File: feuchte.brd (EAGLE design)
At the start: 100 x 80 mm, 23 parts, among them CON1 CON_PCB_7.5MM_3-POLE, CON2 CON_PCB_7.5MM_3-POLE, IC1 IC_ULN2003AD, IC2 ESD_USB_IP4234CZ6, K1 RELAY_G5LA, K2 RELAY_G5LA, Q1 12MHz, U1 MCU_ATMEGA32U2-AU

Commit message: weiter gelayouted
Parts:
- added R4: 1k, Bauelemente:0603
- moved C9 79.0 mm to (74.5, 75.8)
- moved C8 64.0 mm to (72.4, 67.8)
- moved R1 64.0 mm to (70.0, 72.3)
- moved C10 64.0 mm to (75.3, 62.7)
- moved C5 44.0 mm to (38.9, 54.9), turned to 270 degrees
- moved C7 42.1 mm to (65.0, 72.2)
- moved C4 34.2 mm to (43.1, 65.3)
- moved C6 32.0 mm to (43.1, 66.8)
- moved C3 17.7 mm to (54.9, 64.6), turned to 90 degrees
- moved U$1 15.7 mm to (45.7, 45.3), turned to 0 degrees
- moved C2 15.2 mm to (54.9, 68.3)
- moved Q1 12.8 mm to (49.7, 65.7), flipped to the top
- moved U1 8.86 mm to (46.8, 55.8), turned to 270 degrees
- moved R2 2.19 mm to (39.1, 62.3)
- moved R3 2.19 mm to (40.6, 62.3)
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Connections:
- net USBC_N renamed USBC_
- net USBR_N renamed USBR_
- new net N$20: R4.2, U1.13
- net GND: now also IC1.1, IC1.3, IC1.4, IC1.5, IC1.6, R4.1; no longer U1.13
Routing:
- net +5V: track 56.9 -> 69.4 mm, vias 0 -> 1
- net N$1: track 9.75 -> 0.00 mm
- net USBR_P: track 0.00 -> 7.32 mm
- net USBC_P: track 0.35 -> 7.35 mm
- net N$11: track 2.20 -> 9.09 mm
- net N$12: track 9.50 -> 16.0 mm
- net USBR_: track 0.00 -> 6.30 mm
- net N$2: track 6.08 -> 0.00 mm
- net USBC_: track 0.35 -> 6.22 mm
- net +3V3: track 0.00 -> 3.92 mm
- net GND: track 17.0 -> 19.0 mm
- added copper zone on layer 16, net +5V
- added copper zone on layer 16, net GND

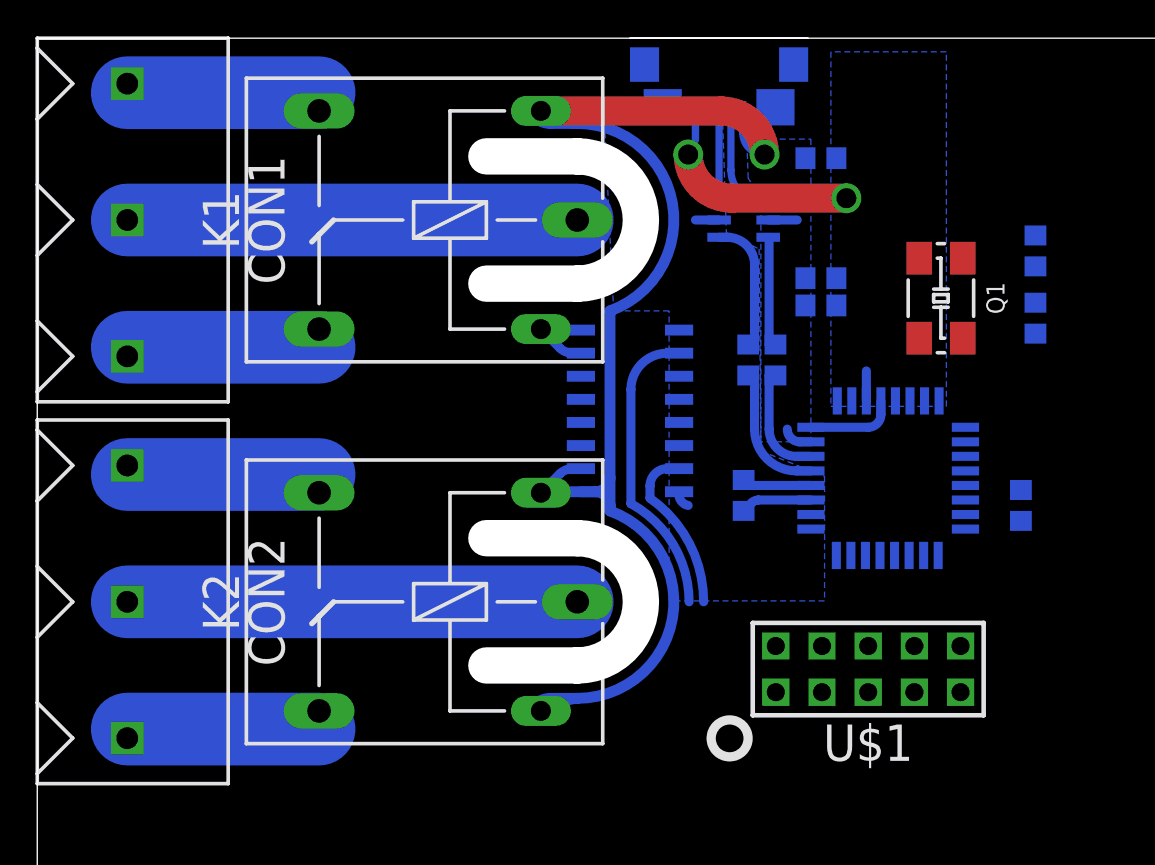
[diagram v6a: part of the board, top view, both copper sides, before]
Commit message: weiter gelayouted, jetzt mit quarz
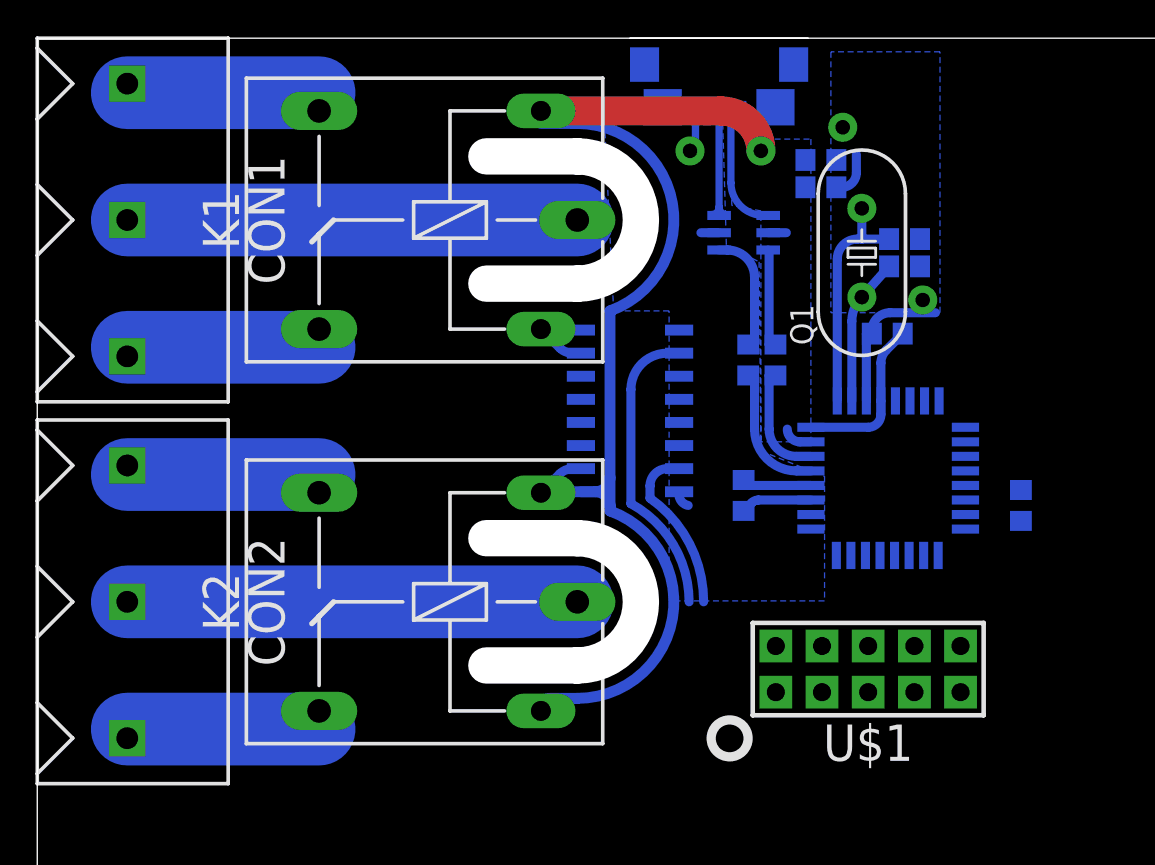
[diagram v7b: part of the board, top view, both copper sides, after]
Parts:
- C1: value 100n -> 10µ
- C6: value 10µ -> 100n
- Q1: value 12MHz -> 16MHz; device Bauelemente:QUARTZ_ABMM2 -> Bauelemente:QUARTZ_HC49S
- moved C3 7.74 mm to (47.7, 67.5), turned to 180 degrees
- moved C2 7.23 mm to (47.7, 69.0), turned to 180 degrees
- moved Q1 5.02 mm to (45.4, 68.2), turned to 90 degrees
- moved C6 5.00 mm to (43.1, 71.8)
- moved C4 3.97 mm to (46.8, 63.8), turned to 0 degrees
- moved IC2 0.70 mm to (38.9, 69.3)
- moved C1 0.10 mm to (43.1, 73.3)
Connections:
- net GND: no longer Q1.2, Q1.4
- net N$1: now also Q1.2; no longer Q1.1
- net N$2: now also Q1.1; no longer Q1.3
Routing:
- net N$1: track 0.00 -> 12.8 mm
- net N$2: track 0.00 -> 8.08 mm
- net +5V: track 69.4 -> 71.0 mm
- net GND: track 19.0 -> 17.9 mm, vias 2 -> 3
- net USBR_P: track 7.32 -> 6.62 mm
- net USBR_: track 6.30 -> 5.60 mm
- net USBCON_N: track 5.92 -> 6.62 mm
- net USBCON_: track 6.06 -> 6.76 mm

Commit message: weiter gelayouted
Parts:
- moved U$1 0.67 mm to (45.4, 44.7)
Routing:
- net +5V: track 71.0 -> 78.3 mm, vias 1 -> 2
- net N$11: track 9.09 -> 4.92 mm
- net N$12: track 16.0 -> 12.5 mm
- net GND: track 17.9 -> 17.0 mm, vias 3 -> 4
- added copper zone on layer 1, net GND
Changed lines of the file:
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@@
 <wire x1="5" y1="56" x2="15.5" y2="56" width="14" layer="42"/>
 <wire x1="5" y1="42" x2="15.5" y2="42" width="14" layer="42"/>
+<wire x1="29.7" y1="49" x2="24.7" y2="49" width="10" layer="41"/>
+<wire x1="29.7" y1="70" x2="24.7" y2="70" width="10" layer="41"/>
+<wire x1="15.5" y1="77" x2="5" y2="77" width="14" layer="41"/>
+<wire x1="5" y1="70" x2="22.4" y2="70" width="14" layer="41"/>
+<rectangle x1="22" y1="63" x2="26.7" y2="65" layer="41"/>
+<rectangle x1="22" y1="75" x2="26.7" y2="77" layer="41"/>
+<wire x1="5" y1="49" x2="22.4" y2="49" width="14" layer="41"/>
+<rectangle x1="22" y1="42" x2="26.7" y2="44" layer="41"/>
+<rectangle x1="22" y1="54" x2="26.7" y2="56" layer="41"/>
+<wire x1="5" y1="63" x2="15.5" y2="63" width="14" layer="41"/>
+<wire x1="5" y1="56" x2="15.5" y2="56" width="14" layer="41"/>
+<wire x1="5" y1="42" x2="15.5" y2="42" width="14" layer="41"/>
 </plain>
 <attributes>
@@
 <element name="USB1" library="Bauelemente" package="CON_MICROUSB_ZX62R-B-5P" value="CON_MICROUSB_ZX62R-B-5P" x="37.5" y="75.2" rot="MR180"/>
 <element name="IC2" library="Bauelemente" package="USB_ESD_IP4234CZ6" value="ESD_USB_IP4234CZ6" x="38.85" y="69.3" rot="MR90"/>
-<element name="U$1" library="Bauelemente" package="CON_ISP_AVR10" value="CON_SPI_AVR10" x="45.7" y="45.3"/>
+<element name="U$1" library="Bauelemente" package="CON_ISP_AVR10" value="CON_SPI_AVR10" x="45.4" y="44.7"/>
 <element name="C7" library="Bauelemente" package="0603" value="100n" x="65" y="72.2" rot="MR0"/>
 <element name="C8" library="Bauelemente" package="0603" value="100n" x="72.4" y="67.8" rot="MR0"/>
@@
 <contactref element="C6" pad="2"/>
 <contactref element="C4" pad="2"/>
-<via x="35.9" y="73.8" extent="1-16" drill="0.8" alwaysstop="yes"/>
+<via x="35.9" y="73.8" extent="1-16" drill="0.8"/>
 <contactref element="U$1" pad="8"/>
 <contactref element="U$1" pad="10"/>
@@
 <vertex x="31.7" y="65"/>
 </polygon>
-<wire x1="35.3" y1="55.055" x2="35.8" y2="54.3" width="0.5" layer="16" curve="90"/>
 <wire x1="42.55" y1="55.4" x2="38.85" y2="55.4" width="0.5" layer="16"/>
 <wire x1="38.85" y1="55.4" x2="38.85" y2="55.7" width="0.5" layer="16"/>
@@
 <polygon width="0.5" layer="16" isolate="0.3">
 <vertex x="43.65" y="79.25"/>
-<vertex x="43.65" y="64.9"/>
+<vertex x="43.65" y="71.3"/>
+<vertex x="45.4" y="71.3"/>
+<vertex x="45.4" y="64.9"/>
 <vertex x="49.65" y="64.9"/>
 <vertex x="49.65" y="79.25"/>
 </polygon>
-<wire x1="48.55" y1="68.95" x2="44.3" y2="75.1" width="0" layer="19" extent="16-16"/>
-<wire x1="48.7" y1="65.6" x2="49.4" y2="64.9" width="0" layer="19" extent="16-16"/>
-<wire x1="42.55" y1="55.4" x2="45.6" y2="60.05" width="0" layer="19" extent="16-16"/>
-<wire x1="43.16" y1="46.57" x2="42.55" y2="55.4" width="0" layer="19" extent="16-16"/>
-<wire x1="45.7" y1="46.57" x2="43.16" y2="46.57" width="0" layer="19" extent="1-1"/>
-<wire x1="48.24" y1="46.57" x2="45.7" y2="46.57" width="0" layer="19" extent="1-1"/>
-<wire x1="50.78" y1="46.57" x2="48.24" y2="46.57" width="0" layer="19" extent="1-1"/>
-<wire x1="54.1" y1="53.45" x2="50.78" y2="46.57" width="0" layer="19" extent="16-16"/>
+<polygon width="0.5" layer="1" isolate="0.5">
+<vertex x="20" y="80"/>
+<vertex x="59.2" y="80" curve="-90"/>
+<vertex x="60" y="79.2"/>
+<vertex x="60" y="39"/>
+<vertex x="20.8" y="39" curve="-90"/>
+<vertex x="20" y="39.8"/>
+</polygon>
+<via x="37.5" y="57.4" extent="1-16" drill="0.8" alwaysstop="yes"/>
+<wire x1="50.48" y1="45.97" x2="54.1" y2="53.45" width="0" layer="19" extent="16-16"/>
 </signal>
 <signal name="N$1">
@@
 <wire x1="40.2" y1="69.3" x2="41.2" y2="69.3" width="0.5" layer="16"/>
 <wire x1="46.69289375" y1="62.84289375" x2="47.6" y2="63.75" width="0.5" layer="16"/>
-<wire x1="29.7" y1="43.69" x2="40.62" y2="46.57" width="0" layer="19" extent="16-16"/>
-<wire x1="38.8" y1="75.5142125" x2="29.7" y2="75.31" width="0" layer="19" extent="16-16"/>
-<wire x1="39.8" y1="73.8" x2="37.6" y2="76" width="1.6" layer="1" curve="90"/>
-<wire x1="37.6" y1="76" x2="27.7" y2="76" width="1.6" layer="1"/>
+<via x="32.1" y="59.5" extent="1-16" drill="0.8" diameter="1.8"/>
+<wire x1="32.1" y1="59.5" x2="36.8" y2="59.5" width="1" layer="1"/>
+<wire x1="36.8" y1="59.5" x2="39.8" y2="62.5" width="1" layer="1" curve="90"/>
+<wire x1="39.8" y1="62.5" x2="39.8" y2="73.8" width="1" layer="1"/>
+<wire x1="29.7" y1="43.69" x2="40.32" y2="45.97" width="0" layer="19" extent="16-16"/>
+<wire x1="32.1" y1="59.5" x2="31.5" y2="55.855" width="0" layer="19" extent="16-16"/>
 </signal>
 <signal name="USBR_P">
@@
 <contactref element="U$1" pad="7"/>
 <contactref element="U1" pad="15"/>
-<wire x1="48.24" y1="44.03" x2="51.05" y2="53.8" width="0" layer="19" extent="16-16"/>
+<wire x1="47.94" y1="43.43" x2="51.05" y2="53.8" width="0" layer="19" extent="16-16"/>
 </signal>
 <signal name="N$4">
 <contactref element="U$1" pad="1"/>
 <contactref element="U1" pad="16"/>
-<wire x1="40.62" y1="44.03" x2="51.05" y2="53" width="0" layer="19" extent="16-16"/>
+<wire x1="40.32" y1="43.43" x2="51.05" y2="53" width="0" layer="19" extent="16-16"/>
 </signal>
 <signal name="N$5">
 <contactref element="U$1" pad="9"/>
 <contactref element="U1" pad="17"/>
-<wire x1="50.78" y1="44.03" x2="49.55" y2="51.55" width="0" layer="19" extent="16-16"/>
+<wire x1="50.48" y1="43.43" x2="49.55" y2="51.55" width="0" layer="19" extent="16-16"/>
 </signal>
 <signal name="N$6">
 <contactref element="U1" pad="24"/>
 <contactref element="U$1" pad="5"/>
-<wire x1="45.7" y1="44.03" x2="43.95" y2="51.55" width="0" layer="19" extent="16-16"/>
+<wire x1="45.4" y1="43.43" x2="43.95" y2="51.55" width="0" layer="19" extent="16-16"/>
 </signal>
 <signal name="N$8">
@@
 <contactref element="U1" pad="23"/>
 <contactref element="IC1" pad="7"/>
-<wire x1="35.3" y1="56.325" x2="34.65" y2="56.325" width="0.5" layer="16"/>
-<wire x1="34.65" y1="56.325" x2="33.7" y2="55.375" width="0.5" layer="16" curve="90"/>
-<wire x1="33.7" y1="55.375" x2="33.7" y2="54.7" width="0.5" layer="16"/>
-<wire x1="36.65" y1="49" x2="33.7" y2="54.7" width="0.5" layer="16" curve="54.940573"/>
-<wire x1="36.65" y1="49" x2="44.75" y2="51.55" width="0" layer="19" extent="16-16"/>
+<wire x1="35.3" y1="56.325" x2="34.6" y2="56.325" width="0.5" layer="16"/>
+<wire x1="34.6" y1="56.325" x2="33.9" y2="55.625" width="0.5" layer="16" curve="90"/>
+<wire x1="33.9" y1="55.625" x2="33.9" y2="54.7" width="0.5" layer="16"/>
+<wire x1="33.9" y1="54.7" x2="34.4" y2="54.2" width="0.5" layer="16" curve="90"/>
+<wire x1="34.4" y1="54.2" x2="36" y2="54.2" width="0.5" layer="16"/>
+<wire x1="36" y1="54.2" x2="44.75" y2="51.55" width="0" layer="19" extent="16-16"/>
 </signal>
 <signal name="N$12">
 <contactref element="U1" pad="21"/>
 <contactref element="IC1" pad="2"/>
-<wire x1="35.3" y1="62.675" x2="34.65" y2="62.675" width="0.5" layer="16"/>
-<wire x1="34.65" y1="62.675" x2="32.65" y2="60.675" width="0.5" layer="16" curve="90"/>
-<wire x1="32.65" y1="60.675" x2="32.65" y2="54.4" width="0.5" layer="16"/>
-<wire x1="35.85" y1="49" x2="32.65" y2="54.4" width="0.5" layer="16" curve="61.352384"/>
-<wire x1="35.85" y1="49" x2="46.35" y2="51.55" width="0" layer="19" extent="16-16"/>
+<wire x1="36" y1="53.4" x2="34.4" y2="53.4" width="0.5" layer="16"/>
+<wire x1="34.4" y1="53.4" x2="33.1" y2="54.7" width="0.5" layer="16" curve="-90"/>
+<wire x1="33.1" y1="54.7" x2="33.1" y2="55.734315625" width="0.5" layer="16"/>
+<wire x1="33.1" y1="55.734315625" x2="33.5" y2="56.7" width="0.5" layer="16" curve="-45"/>
+<wire x1="33.5" y1="56.7" x2="33.9" y2="57.665684375" width="0.5" layer="16" curve="45"/>
+<wire x1="33.9" y1="57.665684375" x2="33.9" y2="61.875" width="0.5" layer="16"/>
+<wire x1="33.9" y1="61.875" x2="34.7" y2="62.675" width="0.5" layer="16" curve="-90"/>
+<wire x1="34.7" y1="62.675" x2="35.3" y2="62.675" width="0.5" layer="16"/>
+<wire x1="36" y1="53.4" x2="46.35" y2="51.55" width="0" layer="19" extent="16-16"/>
 </signal>
 <signal name="N$20">
@@
 <wire x1="51.05" y1="55.4" x2="54.1" y2="55.15" width="0" layer="19" extent="16-16"/>
 </signal>
+<signal name="N$21">
+</signal>
 </signals>
